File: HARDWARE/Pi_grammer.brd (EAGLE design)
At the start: 63.5 x 78.7 mm, 27 parts, among them U1 AT42QT1010SOT23

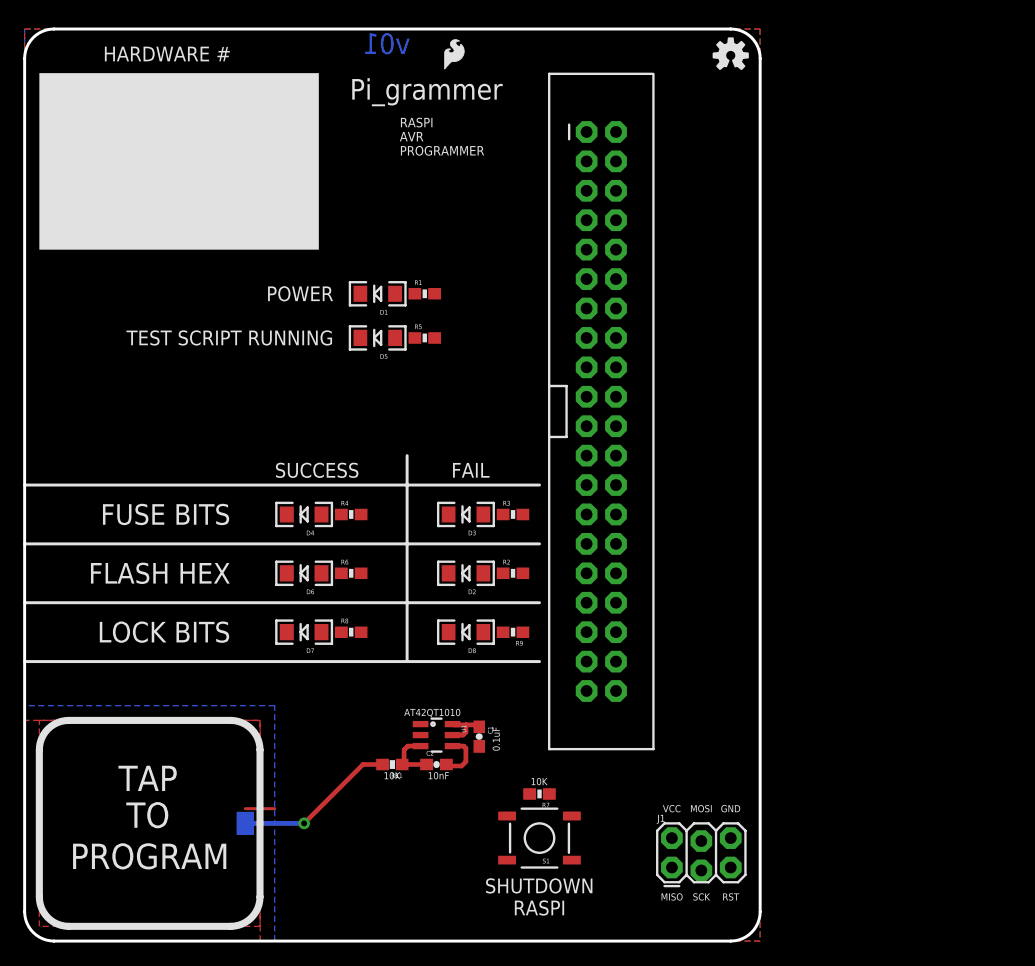
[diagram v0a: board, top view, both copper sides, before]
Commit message: routed
also added .job and .pro to gitignore - eagle auto routing files
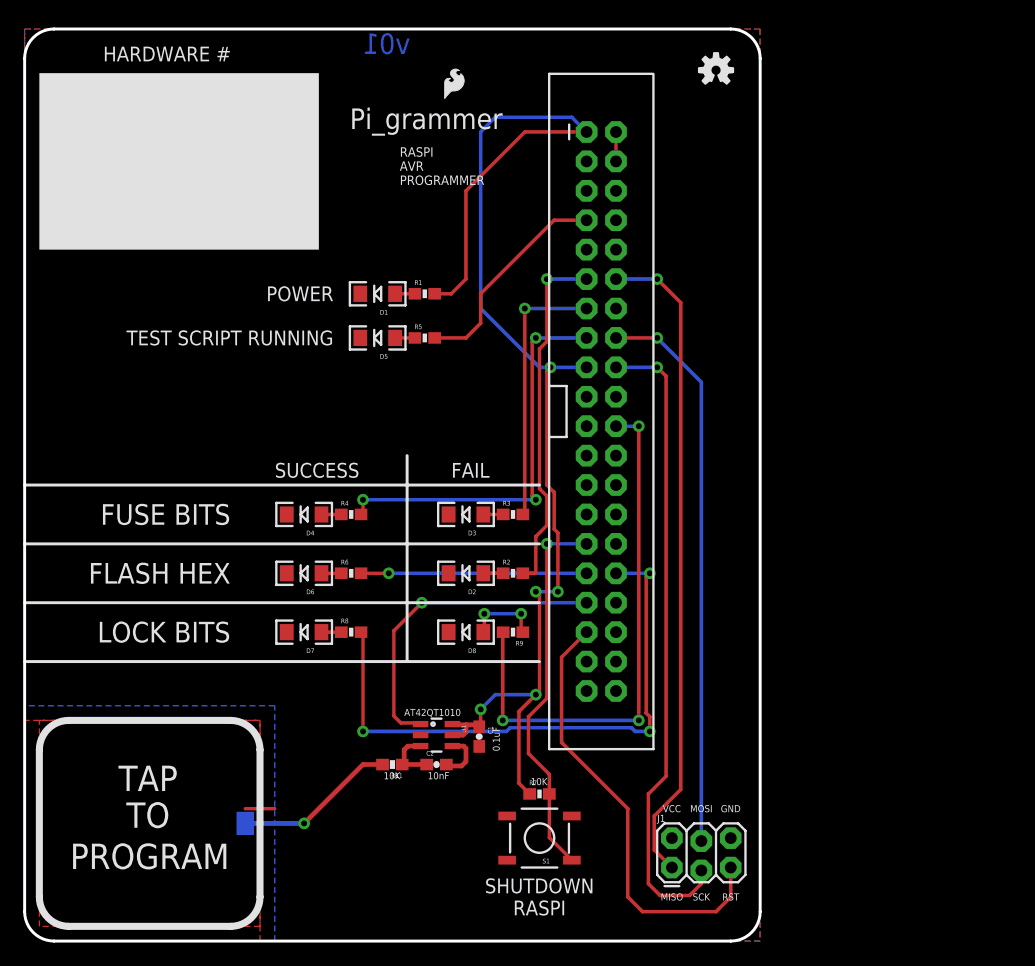
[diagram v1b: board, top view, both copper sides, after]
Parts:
- moved LOGO1 2.54 mm to (35.9, 72.4)
- moved LOGO2 1.80 mm to (59.7, 75.2)
- turned R7 to 0 degrees
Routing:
- net 3.3V: track 4.31 -> 111.9 mm, vias 0 -> 5
- net GP18: track 0.00 -> 56.8 mm, vias 0 -> 1
- net GP24: track 0.00 -> 55.6 mm, vias 0 -> 1
- net LOCK_BITS_PASS: track 0.00 -> 50.6 mm, vias 0 -> 3
- net GP23: track 0.00 -> 48.6 mm, vias 0 -> 1
- net LOCK_BITS_FAIL: track 0.00 -> 46.8 mm, vias 0 -> 3
- net GP19: track 0.00 -> 38.6 mm
- net FUSE_BITS_PASS: track 0.00 -> 35.0 mm, vias 0 -> 3
- net SHUTDOWN: track 0.00 -> 32.9 mm, vias 0 -> 1
- net FLASH_HEX_FAIL: track 0.00 -> 30.9 mm, vias 0 -> 1
- net CAPSENSE: track 0.00 -> 27.8 mm, vias 0 -> 1
- net FUSE_BITS_FAIL: track 0.00 -> 23.3 mm, vias 0 -> 1
- net FLASH_HEX_PASS: track 0.00 -> 19.5 mm, vias 0 -> 1
- net SCRIPT: track 0.00 -> 18.8 mm
- net N$8: track 0.00 -> 6.59 mm, vias 0 -> 2
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
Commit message: Corrected capsense pad to be on top layer
whoops
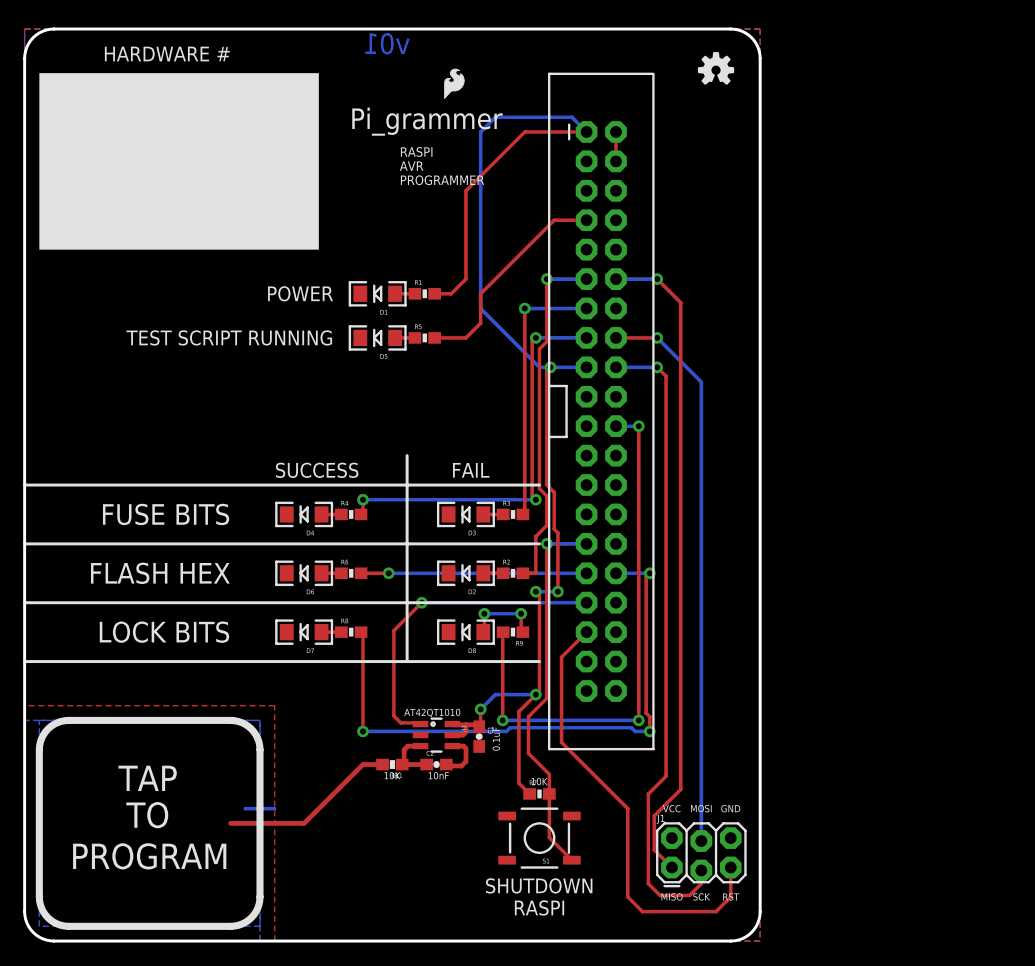
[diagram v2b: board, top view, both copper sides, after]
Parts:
- removed JP9: M01SMD-4.5X1.5, SparkFun-Connectors:PAD-1.5X4.5
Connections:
- net PAD: no longer JP9.P$1
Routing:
- net PAD: track 14.0 -> 15.2 mm, vias 1 -> 0
- added copper zone on layer 1, net PAD
- removed copper zone on layer 16, net PAD
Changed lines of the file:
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@@
 <element name="C2" library="SparkFun-Capacitors" package="0603-CAP" value="10nF" x="35.56" y="15.24"/>
 <element name="R11" library="SparkFun-Resistors" package="0603-RES" value="10k" x="31.75" y="15.24" rot="R180"/>
-<element name="JP9" library="SparkFun-Connectors" package="PAD-1.5X4.5" value="M01SMD-4.5X1.5" x="19.05" y="10.16" rot="MR0"/>
 <element name="J1" library="SparkFun-Connectors" package="2X3_LOCK" value="" x="55.88" y="6.35"/>
 <element name="D8" library="SparkFun-LED" package="LED-1206" value="RED" x="38.1" y="26.67" rot="R180"/>
@@
 <vertex x="63.5" y="78.74"/>
 <vertex x="63.5" y="0"/>
-<vertex x="21.59" y="0"/>
-<vertex x="21.59" y="20.32"/>
-<vertex x="0" y="20.32"/>
+<vertex x="20.32" y="0"/>
+<vertex x="20.32" y="19.05"/>
+<vertex x="0" y="19.05"/>
 </polygon>
 <polygon width="0.381" layer="1" isolate="0.381">
@@
 <vertex x="63.5" y="78.74"/>
 <vertex x="63.5" y="0"/>
-<vertex x="20.32" y="0"/>
-<vertex x="20.32" y="19.05"/>
-<vertex x="0" y="19.05"/>
+<vertex x="21.59" y="0"/>
+<vertex x="21.59" y="20.32"/>
+<vertex x="0" y="20.32"/>
 </polygon>
 <contactref element="D1" pad="C"/>
@@
 <contactref element="C1" pad="2"/>
 <contactref element="U1" pad="2"/>
-<polygon width="0.3048" layer="1" pour="hatch" isolate="0.3048">
+<polygon width="0.3048" layer="16" pour="hatch" isolate="0.3048">
 <vertex x="20.32" y="1.27"/>
 <vertex x="1.27" y="1.27"/>
@@
 <vertex x="20.32" y="19.05"/>
 </polygon>
-<wire x1="21.59" y1="11.43" x2="19.05" y2="11.43" width="0.3048" layer="1"/>
+<wire x1="21.59" y1="11.43" x2="19.05" y2="11.43" width="0.3048" layer="16"/>
 <contactref element="J1" pad="6"/>
 <contactref element="D8" pad="C"/>
@@
 <signal name="PAD">
 <contactref element="R11" pad="2"/>
-<contactref element="JP9" pad="P$1"/>
-<polygon width="0.3048" layer="16" isolate="0.3048">
+<polygon width="0.3048" layer="1" isolate="0.3048">
 <vertex x="20.32" y="16.51" curve="90"/>
 <vertex x="17.78" y="19.05"/>
@@
 <wire x1="30.9" y1="15.24" x2="29.21" y2="15.24" width="0.4064" layer="1"/>
 <wire x1="29.21" y1="15.24" x2="24.13" y2="10.16" width="0.4064" layer="1"/>
-<via x="24.13" y="10.16" extent="1-16" drill="0.508"/>
-<wire x1="24.13" y1="10.16" x2="19.05" y2="10.16" width="0.4064" layer="16"/>
+<wire x1="24.13" y1="10.16" x2="17.78" y2="10.16" width="0.4064" layer="1"/>
 </signal>
 <signal name="CAPSENSE">

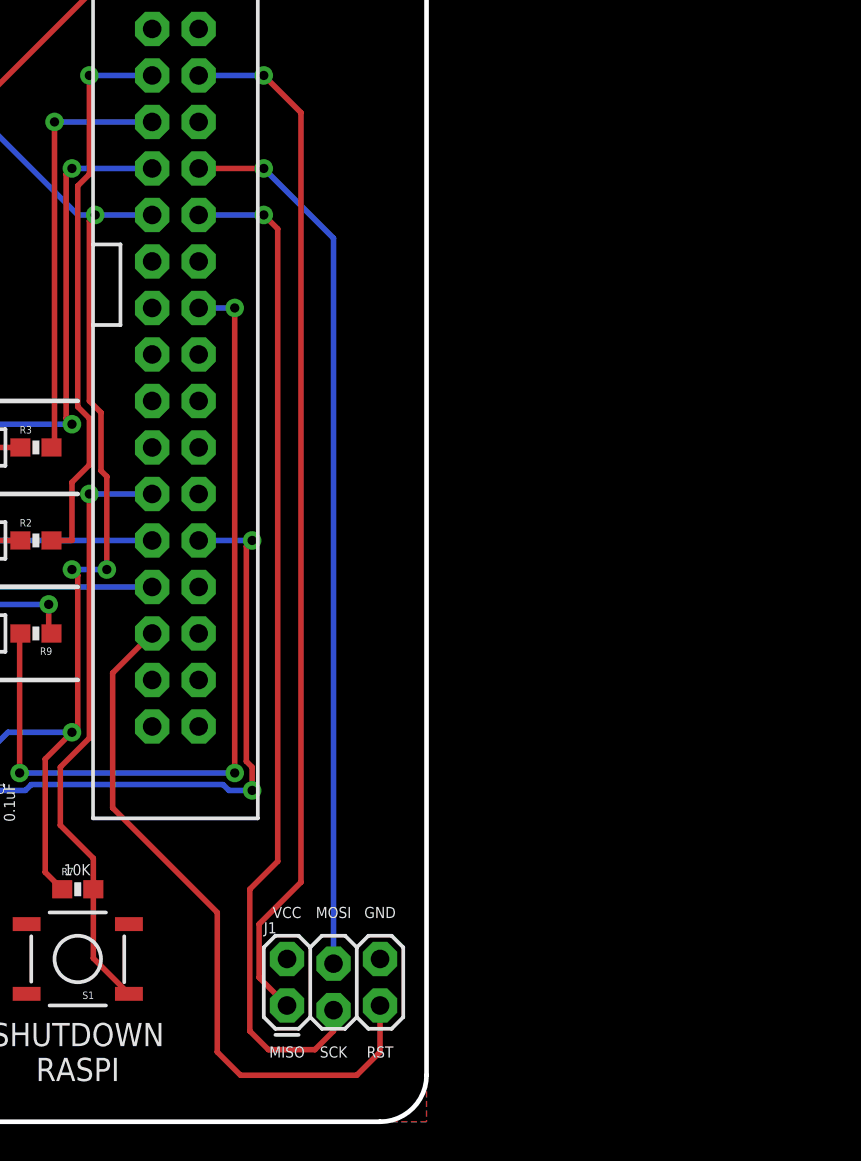
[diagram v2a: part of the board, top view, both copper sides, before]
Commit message: Moved ICSP lines to a 1x6 connector
Also created adapter from 1x6 cable to 3x2 header
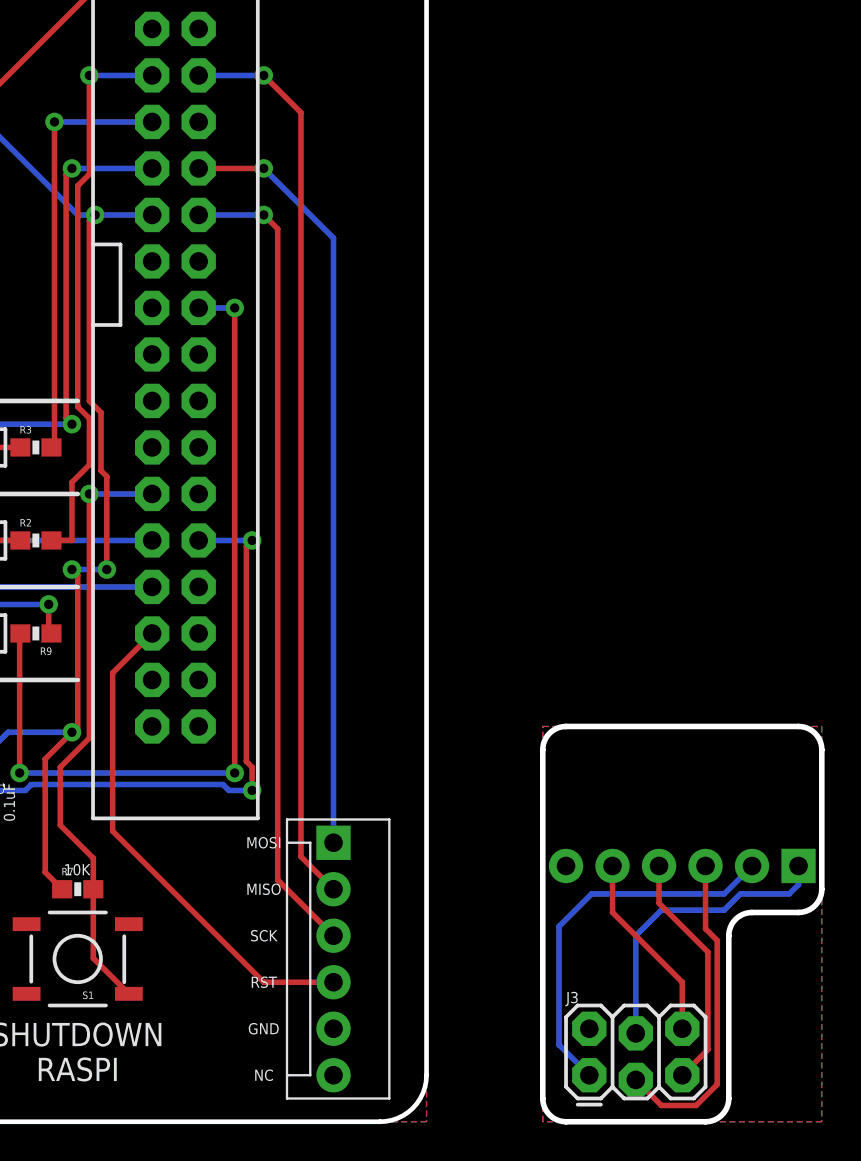
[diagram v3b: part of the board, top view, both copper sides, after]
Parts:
- removed J1: (no value), SparkFun-Connectors:2X3_LOCK
- added J2: TARGET_copy, SparkFun-Connectors:MOLEX-1X6
- added J3: TESTBED, SparkFun-Connectors:2X3_LOCK
- added J4: CABLE, SparkFun-Connectors:MOLEX-1X6-RA
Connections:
- removed net GP18: J1.1, JP2.12
- removed net GP19: J1.5, JP2.35
- removed net GP23: J1.4, JP2.16
- removed net GP24: J1.3, JP2.18
- new net GND_C: J3.6, J4.5
- new net MISO_C: J3.1, J4.2
- new net MISO_T: J2.2, JP2.12
- new net MOSI_C: J3.4, J4.1
- new net MOSI_T: J2.1, JP2.16
- new net RST_C: J3.5, J4.4
- new net RST_T: J2.4, JP2.35
- new net SCK_C: J3.3, J4.3
- new net SCK_T: J2.3, JP2.18
- net GND: now also J2.5; no longer J1.6
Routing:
- net GP18: track 56.8 -> 0.00 mm, vias 1 -> 0
- net GP24: track 55.6 -> 0.00 mm, vias 1 -> 0
- net MISO_T: track 0.00 -> 49.6 mm, vias 0 -> 1
- net GP23: track 48.6 -> 0.00 mm, vias 1 -> 0
- net SCK_T: track 0.00 -> 44.5 mm, vias 0 -> 1
- net MOSI_T: track 0.00 -> 42.0 mm, vias 0 -> 1
- net GP19: track 38.6 -> 0.00 mm
- net RST_T: track 0.00 -> 27.2 mm
- net MISO_C: track 0.00 -> 20.7 mm
- net SCK_C: track 0.00 -> 17.7 mm
- net MOSI_C: track 0.00 -> 16.4 mm
- net RST_C: track 0.00 -> 13.1 mm
- net GND_C: track 0.00 -> 10.5 mm
- added copper zone on layer 1, net GND_C
- added copper zone on layer 16, net GND_C
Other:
- board size 63.5 x 78.7 mm -> 85.1 x 78.7 mm
- board text added: "NC"
- board text removed: "VCC"
